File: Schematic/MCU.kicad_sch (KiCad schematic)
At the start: 21 parts, among them IC3 STM32H743VIT6, SW1 TS24CA, Y1 8MHz

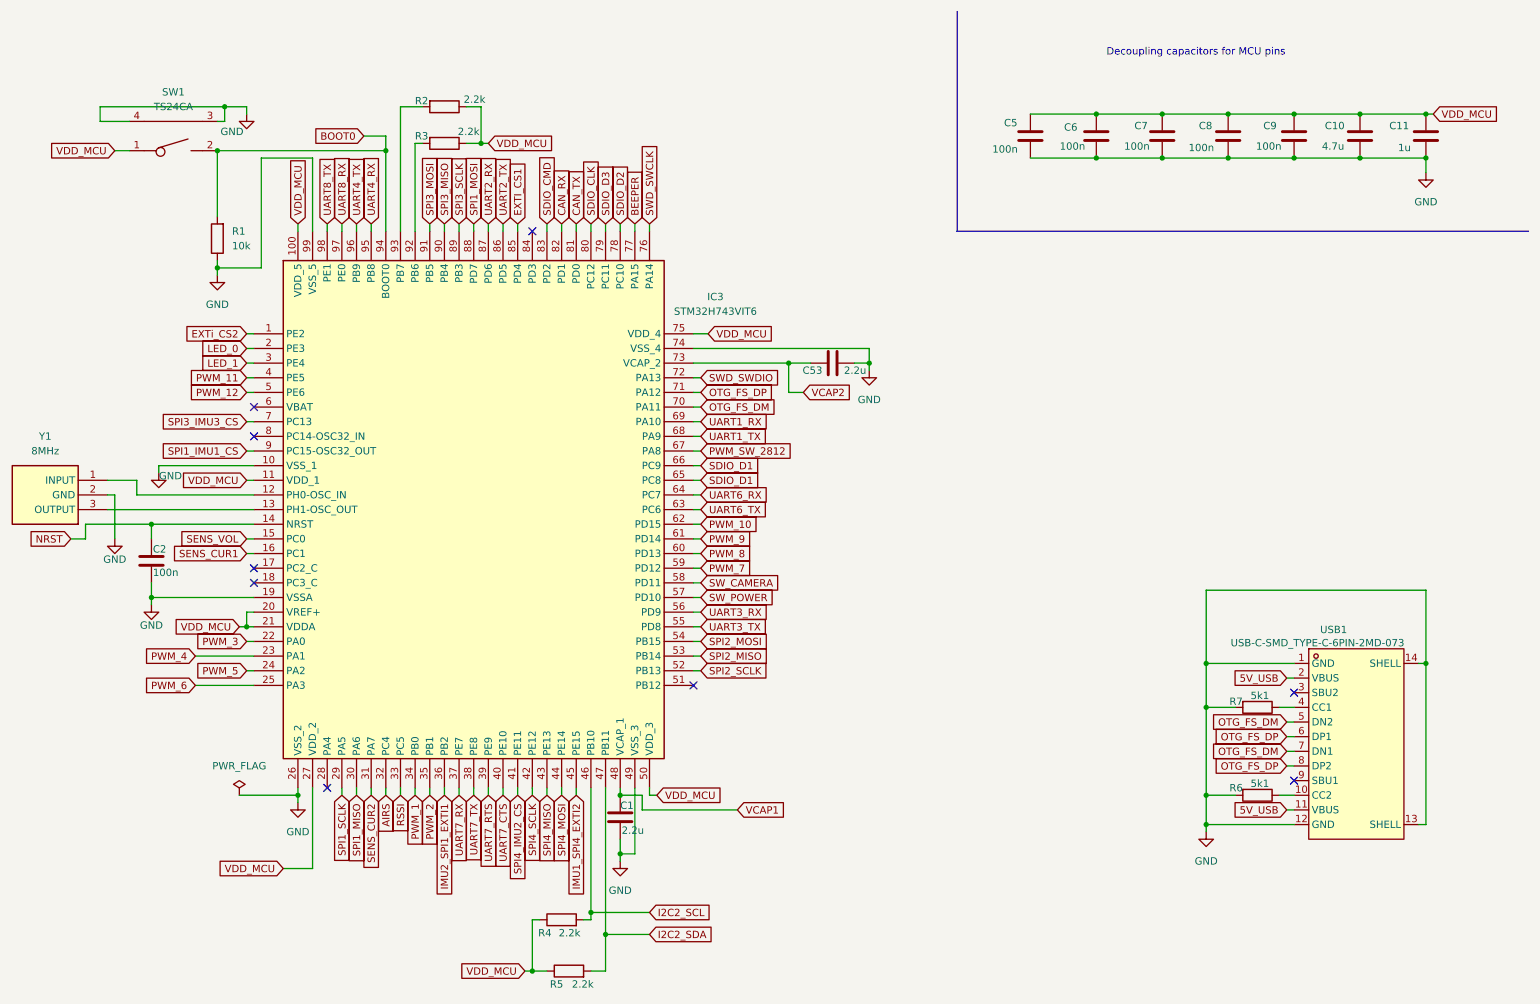
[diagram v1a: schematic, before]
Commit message: Refactor schematic files and add net definitions
- Updated priority values for GND and POWER net classes in fch7.kicad_pro.
- Added USB_DIFF net class with associated patterns for USB differential signals.
- Removed duplicate junctions and adjusted wire connections in rf_rx.kicad_sch for clarity.
- Adjusted component positions and properties in rf_rx.kicad_sch for better layout.
- Modified text positions for IMU components in sensors.kicad_sch to improve readability.
- Cleaned up unnecessary wires and added new connections in sensors.kicad_sch.
- Introduced nets.txt file to define various electrical nets used across the schematics.
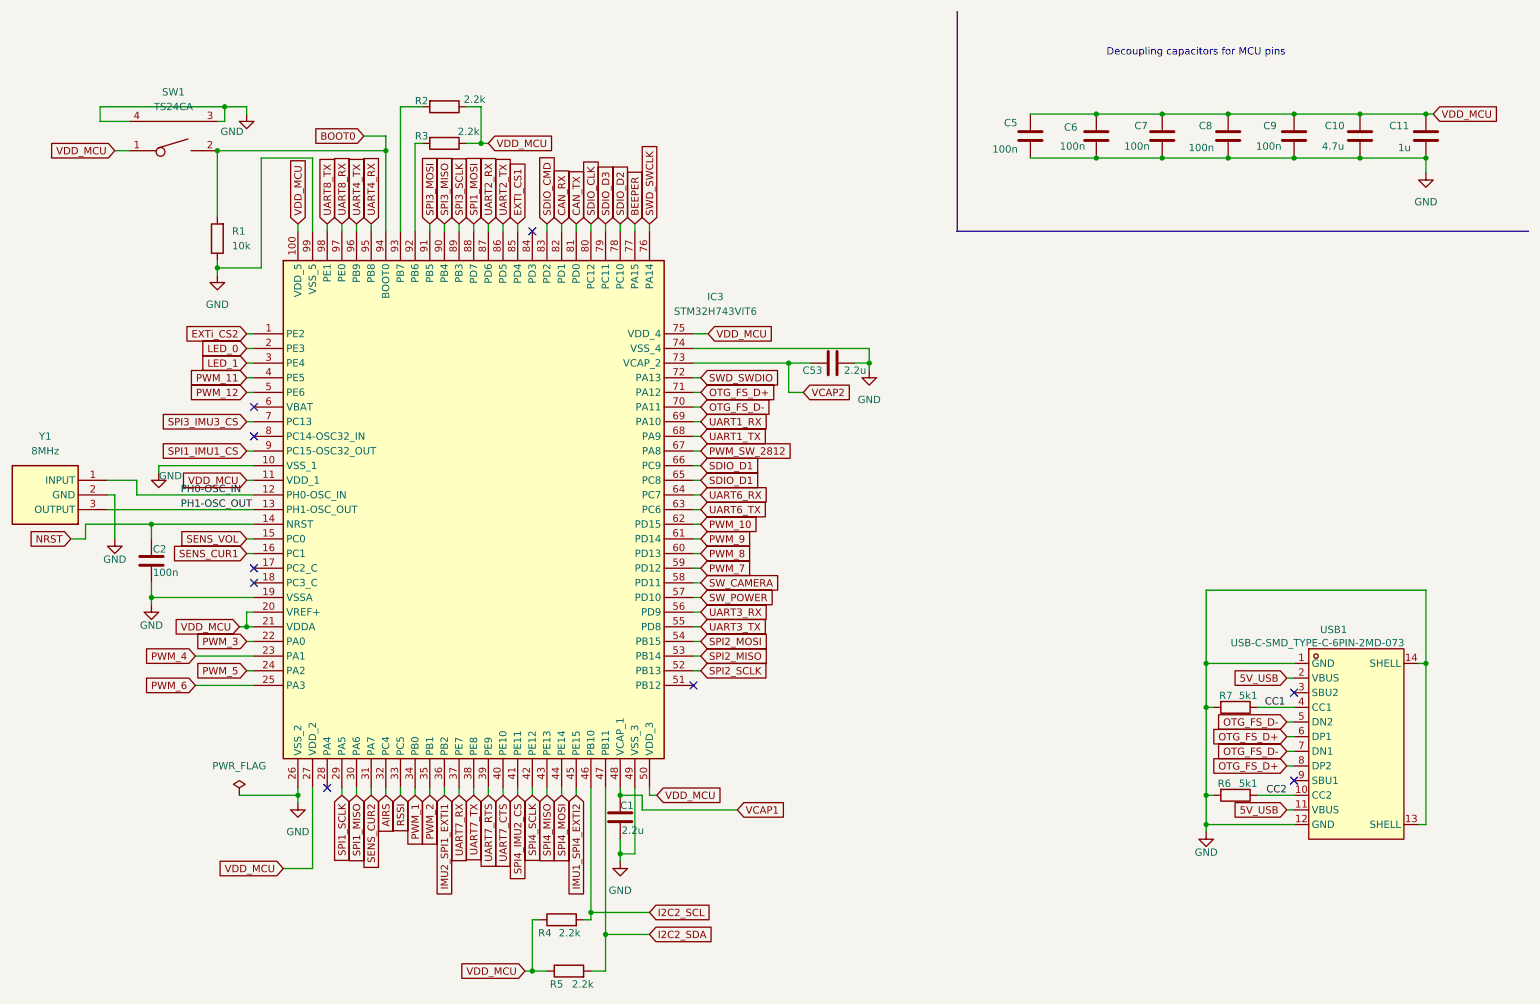
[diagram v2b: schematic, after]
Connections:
- net CC2: now reaches R6.1, USB1.10 (CC2)
- net CC1: now reaches R7.1, USB1.4 (CC1)
- net PH0-OSC_IN: now reaches IC3.12 (PH0-OSC_IN), Y1.1 (INPUT)
- net PH1-OSC_OUT: now reaches IC3.13 (PH1-OSC_OUT), Y1.3 (OUTPUT)
- net OTG_FS_DM renamed OTG_FS_D-
- net OTG_FS_DP renamed OTG_FS_D+
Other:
- moved on the sheet: R6, R7
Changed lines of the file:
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@@
 	)
 	(junction
-		(at 57.15 36.83)
+		(at 228.6 148.59)
 		(diameter 0)
 		(color 0 0 0 0)
 	)
 	(junction
-		(at 255.27 30.48)
+		(at 57.15 36.83)
 		(diameter 0)
 		(color 0 0 0 0)
 	)
 	(junction
-		(at 220.98 38.1)
+		(at 255.27 30.48)
 		(diameter 0)
 		(color 0 0 0 0)
 	)
 	(junction
-		(at 156.21 73.66)
+		(at 220.98 38.1)
 		(diameter 0)
 		(color 0 0 0 0)
 	)
 	(junction
-		(at 228.6 133.35)
+		(at 156.21 73.66)
 		(diameter 0)
 		(color 0 0 0 0)
@@
 	)
 	(junction
+		(at 228.6 133.35)
+		(diameter 0)
+		(color 0 0 0 0)
+	)
+	(junction
 		(at 209.55 38.1)
 		(diameter 0)
@@
 	)
 	(junction
-		(at 228.6 148.59)
-		(diameter 0)
-		(color 0 0 0 0)
-	)
-	(junction
 		(at 45.72 101.6)
 		(diameter 0)
@@
 	(wire
 		(pts
+			(xy 237.49 133.35) (xy 243.84 133.35)
+		)
+		(stroke
+			(width 0)
+			(type default)
+		)
+	)
+	(wire
+		(pts
 			(xy 170.18 73.66) (xy 170.18 74.93)
 		)
@@
 	(wire
 		(pts
-			(xy 241.3 133.35) (xy 243.84 133.35)
-		)
-		(stroke
-			(width 0)
-			(type default)
-		)
-	)
-	(wire
-		(pts
 			(xy 127 156.21) (xy 127 158.75)
 		)
@@
 	(wire
 		(pts
-			(xy 228.6 148.59) (xy 233.68 148.59)
-		)
-		(stroke
-			(width 0)
-			(type default)
-		)
-	)
-	(wire
-		(pts
 			(xy 255.27 30.48) (xy 266.7 30.48)
 		)
@@
 	(wire
 		(pts
+			(xy 228.6 133.35) (xy 228.6 148.59)
+		)
+		(stroke
+			(width 0)
+			(type default)
+		)
+	)
+	(wire
+		(pts
 			(xy 266.7 113.03) (xy 228.6 113.03)
 		)
@@
 	(wire
 		(pts
-			(xy 228.6 125.73) (xy 228.6 133.35)
+			(xy 228.6 148.59) (xy 228.6 153.67)
 		)
 		(stroke
@@
 	(wire
 		(pts
+			(xy 228.6 148.59) (xy 229.87 148.59)
+		)
+		(stroke
+			(width 0)
+			(type default)
+		)
+	)
+	(wire
+		(pts
 			(xy 73.66 38.1) (xy 64.77 38.1)
 		)
@@
 	(wire
 		(pts
-			(xy 228.6 133.35) (xy 228.6 148.59)
-		)
-		(stroke
-			(width 0)
-			(type default)
-		)
-	)
-	(wire
-		(pts
 			(xy 170.18 71.12) (xy 170.18 73.66)
 		)
@@
 	(wire
 		(pts
-			(xy 228.6 148.59) (xy 228.6 153.67)
+			(xy 228.6 125.73) (xy 228.6 133.35)
 		)
 		(stroke
@@
 	(wire
 		(pts
-			(xy 167.64 73.66) (xy 170.18 73.66)
+			(xy 228.6 133.35) (xy 229.87 133.35)
 		)
 		(stroke
@@
 	(wire
 		(pts
-			(xy 228.6 133.35) (xy 233.68 133.35)
+			(xy 167.64 73.66) (xy 170.18 73.66)
 		)
 		(stroke
@@
 	(wire
 		(pts
+			(xy 237.49 148.59) (xy 243.84 148.59)
+		)
+		(stroke
+			(width 0)
+			(type default)
+		)
+	)
+	(wire
+		(pts
 			(xy 106.68 49.53) (xy 106.68 50.8)
 		)
@@
 	(wire
 		(pts
-			(xy 241.3 148.59) (xy 243.84 148.59)
+			(xy 43.18 96.52) (xy 63.5 96.52)
 		)
 		(stroke
@@
 		)
 	)
-	(wire
-		(pts
-			(xy 43.18 96.52) (xy 63.5 96.52)
+	(label "CC2"
+		(at 242.57 148.59 180)
+		(effects
+			(font
+				(size 1.27 1.27)
+			)
+			(justify right bottom)
 		)
-		(stroke
-			(width 0)
-			(type default)
+	)
+	(label "CC1"
+		(at 238.76 133.35 0)
+		(effects
+			(font
+				(size 1.27 1.27)
+			)
+			(justify left bottom)
+		)
+	)
+	(label "PH0-OSC_IN"
+		(at 50.8 96.52 0)
+		(effects
+			(font
+				(size 1.27 1.27)
+			)
+			(justify left bottom)
+		)
+	)
+	(label "PH1-OSC_OUT"
+		(at 50.8 99.06 0)
+		(effects
+			(font
+				(size 1.27 1.27)
+			)
+			(justify left bottom)
 		)
 	)
@@
 		)
 	)
-	(global_label "OTG_FS_DM"
+	(global_label "OTG_FS_D-"
 		(shape input)
 		(at 242.57 140.97 180)
@@
 		)
 		(property "Intersheetrefs" "${INTERSHEET_REFS}"
-			(at 229.062 140.97 0)
+			(at 228.941 140.97 0)
 			(effects
 				(font
@@
 		)
 	)
-	(global_label "OTG_FS_DM"
+	(global_label "OTG_FS_D-"
 		(shape input)
 		(at 242.57 135.89 180)
@@
 		)
 		(property "Intersheetrefs" "${INTERSHEET_REFS}"
-			(at 229.062 135.89 0)
+			(at 228.941 135.89 0)
 			(effects
 				(font
@@
 		)
 	)
-	(global_label "OTG_FS_DP"
+	(global_label "OTG_FS_D+"
 		(shape input)
 		(at 242.57 138.43 180)
@@
 		)
 		(property "Intersheetrefs" "${INTERSHEET_REFS}"
-			(at 229.2434 138.43 0)
+			(at 228.941 138.43 0)
 			(effects
 				(font
@@
 		)
 	)
-	(global_label "OTG_FS_DP"
+	(global_label "OTG_FS_D+"
 		(shape input)
 		(at 242.57 143.51 180)
@@
 		)
 		(property "Intersheetrefs" "${INTERSHEET_REFS}"
-			(at 229.2434 143.51 0)
+			(at 228.941 143.51 0)
 			(effects
 				(font
@@
 		)
 	)
-	(global_label "OTG_FS_DM"
+	(global_label "OTG_FS_D-"
 		(shape input)
 		(at 140.97 81.28 0)
@@
 		)
 		(property "Intersheetrefs" "${INTERSHEET_REFS}"
-			(at 154.478 81.28 0)
+			(at 154.599 81.28 0)
 			(effects
 				(font
@@
 		)
 	)
-	(global_label "OTG_FS_DP"
+	(global_label "OTG_FS_D+"
 		(shape input)
 		(at 140.97 78.74 0)
@@
 		)
 		(property "Intersheetrefs" "${INTERSHEET_REFS}"
-			(at 154.2966 78.74 0)
+			(at 154.599 78.74 0)
 			(effects
 				(font
@@
 		(on_board yes)
 		(dnp no)
-		(fields_autoplaced yes)
 		(property "Reference" "#PWR07"
 			(at 228.6 161.29 0)
@@
 		)
 		(property "Value" "GND"
-			(at 228.6 160.02 0)
+			(at 228.6 158.496 0)
 			(effects
 				(font
@@
 	(symbol
 		(lib_id "Device:R")
-		(at 237.49 133.35 270)
+		(at 233.68 133.35 270)
 		(unit 1)
 		(exclude_from_sim no)
@@
 		(dnp no)
 		(property "Reference" "R7"
-			(at 234.95 132.334 90)
+			(at 233.172 131.318 90)
 			(effects
 				(font
@@
 		)
 		(property "Value" "5k1"
-			(at 239.522 131.318 90)
+			(at 237.49 131.318 90)
 			(effects
 				(font
@@
 		)
 		(property "Footprint" "Resistor_SMD:R_0603_1608Metric"
-			(at 237.49 131.572 90)
+			(at 233.68 131.572 90)
 			(effects
 				(font
@@
 		)
 		(property "Datasheet" "https://www.lcsc.com/datasheet/C23186.pdf"
-			(at 237.49 133.35 0)
+			(at 233.68 133.35 0)
 			(effects
 				(font
@@
 		)
 		(property "Description" "Resistor"
-			(at 237.49 133.35 0)
+			(at 233.68 133.35 0)
 			(effects
 				(font
@@
 		)
 		(property "Fréquence" ""
-			(at 237.49 133.35 90)
+			(at 233.68 133.35 90)
 			(effects
 				(font
@@
 		)
 		(property "MPN" "0603WAF5101T5E"
-			(at 237.49 133.35 90)
+			(at 233.68 133.35 90)
 			(effects
 				(font
@@
 		)
 		(property "Manufacturer" "UNI-ROYAL"
-			(at 237.49 133.35 90)
+			(at 233.68 133.35 90)
 			(effects
 				(font
@@
 	(symbol
 		(lib_id "Device:R")
-		(at 237.49 148.59 270)
+		(at 233.68 148.59 270)
 		(unit 1)
 		(exclude_from_sim no)
@@
 		(dnp no)
 		(property "Reference" "R6"
-			(at 234.95 147.32 90)
+			(at 232.918 146.558 90)
 			(effects
 				(font
@@
 		)
 		(property "Value" "5k1"
-			(at 239.522 146.558 90)
+			(at 237.49 146.558 90)
 			(effects
 				(font
@@
 		)
 		(property "Footprint" "Resistor_SMD:R_0603_1608Metric"
-			(at 237.49 146.812 90)
+			(at 233.68 146.812 90)
 			(effects
 				(font
@@
 		)
 		(property "Datasheet" "https://www.lcsc.com/datasheet/C23186.pdf"
-			(at 237.49 148.59 0)
+			(at 233.68 148.59 0)
 			(effects
 				(font
@@
 		)
 		(property "Description" "Resistor"
-			(at 237.49 148.59 0)
+			(at 233.68 148.59 0)
 			(effects
 				(font
@@
 		)
 		(property "Fréquence" ""
-			(at 237.49 148.59 90)
+			(at 233.68 148.59 90)
 			(effects
 				(font
@@
 		)
 		(property "MPN" "0603WAF5101T5E"
-			(at 237.49 148.59 90)
+			(at 233.68 148.59 90)
 			(effects
 				(font
@@
 		)
 		(property "Manufacturer" "UNI-ROYAL"
-			(at 237.49 148.59 90)
+			(at 233.68 148.59 90)
 			(effects
 				(font

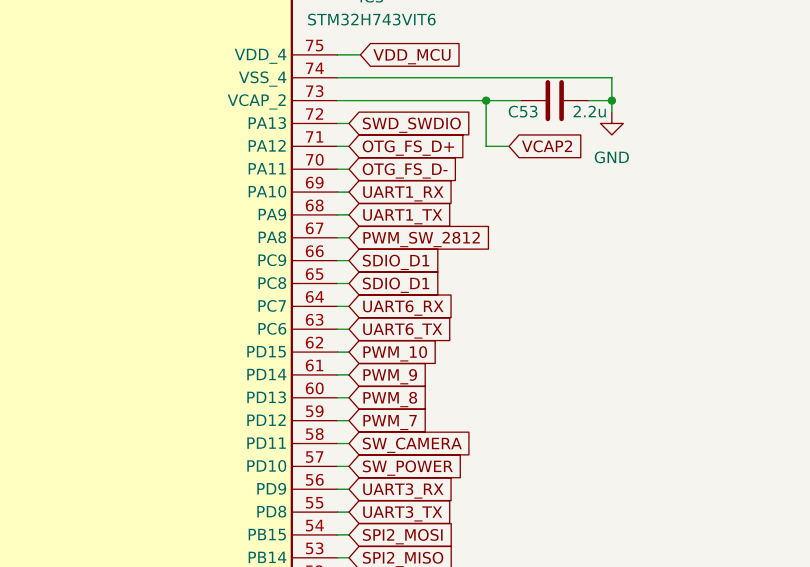
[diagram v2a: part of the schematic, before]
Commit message: Update global label for SDIO and modify wire connections in blackbox LED schematic
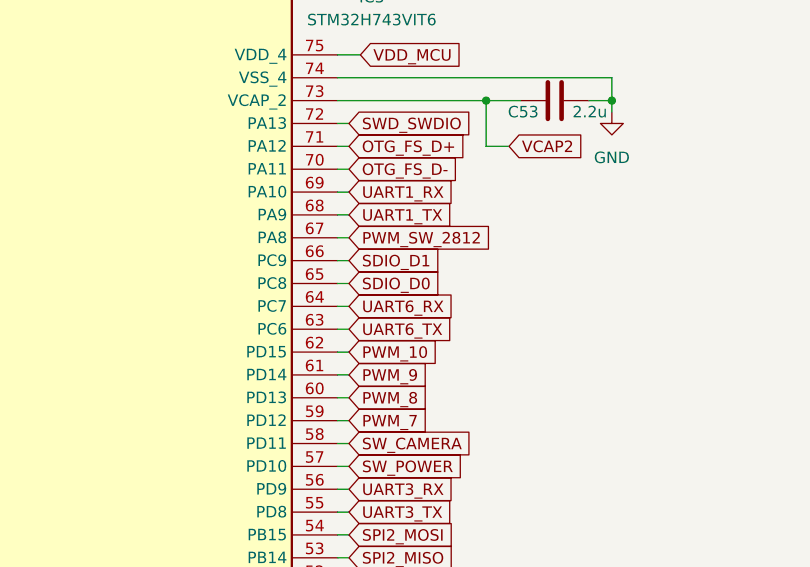
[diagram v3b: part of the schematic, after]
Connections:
- net SDIO_D1: no longer IC3.65 (PC8)
- new net SDIO_D0: IC3.65 (PC8)
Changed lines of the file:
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@@
 		)
 	)
-	(global_label "SDIO_D1"
+	(global_label "SDIO_D0"
 		(shape input)
 		(at 140.97 93.98 0)
